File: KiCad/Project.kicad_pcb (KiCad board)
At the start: 2 copper layers, 74.9 x 99.1 mm, 74 parts, among them IC1 ATMEGA328-P, IC2 ATTINY85-P, IC3 ATTINY85-P, M1 Motor, M2 Motor, P1 CONN_02X03, P2 CONN_01X02, P3 CONN_01X02, P4 CONN_01X02, P5 CONN_02X04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

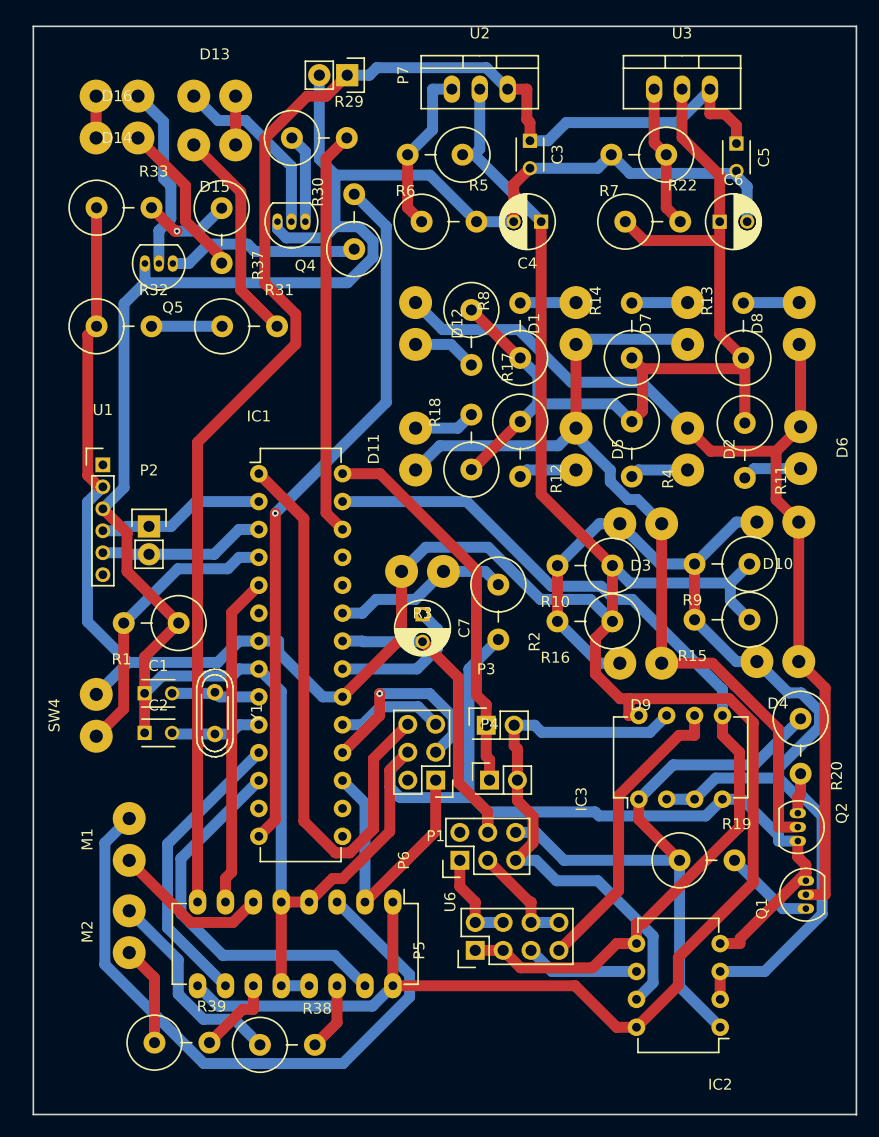
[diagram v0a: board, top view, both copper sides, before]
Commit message: Updated code for BT pairing and modified vias in PCB
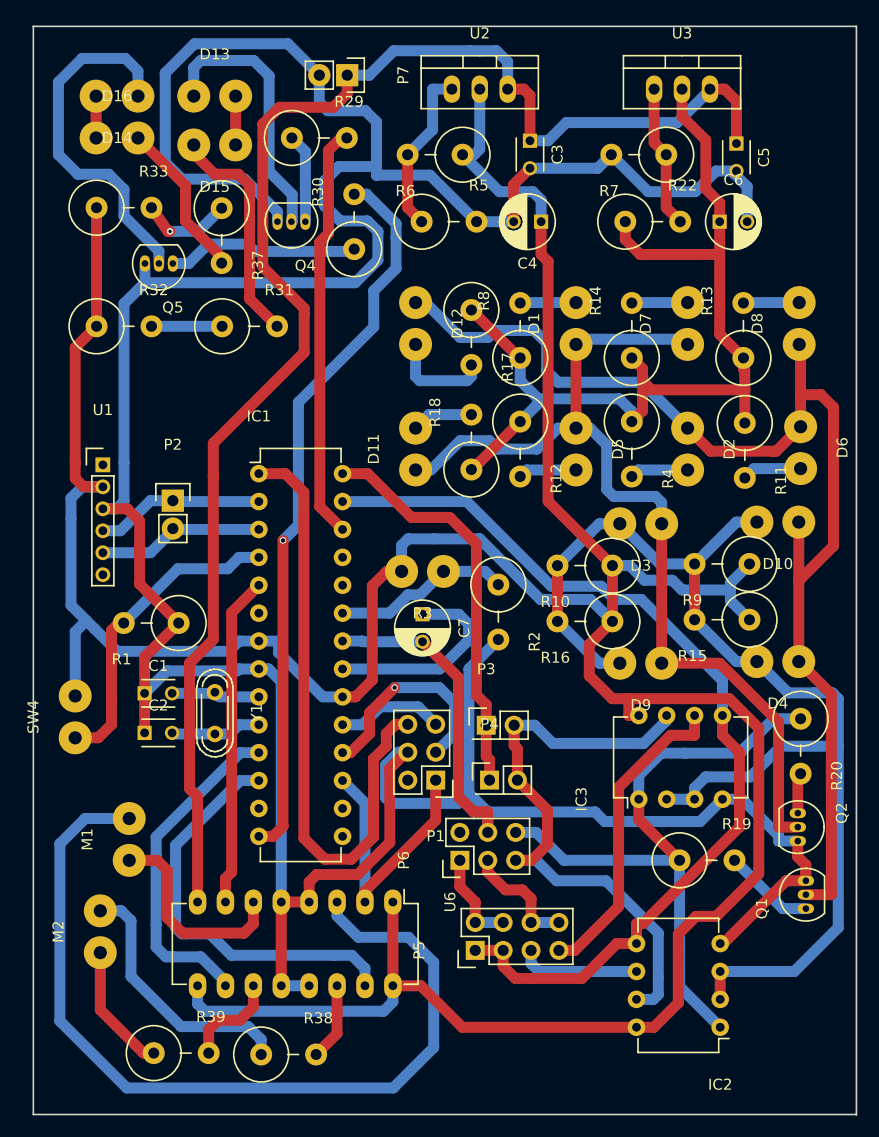
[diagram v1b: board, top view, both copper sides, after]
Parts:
- moved P2 3.19 mm to (64.8, 73.7)
- moved M2 2.63 mm to (58.2, 112.9)
- moved SW4 1.93 mm to (55.9, 93.3)
- moved R39 0.95 mm to (65.5, 124.0)
- moved R38 0.89 mm to (75.3, 124.1)
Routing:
- net GND: track 312.9 -> 358.8 mm
- net /Motor/Vroom: track 59.6 -> 81.1 mm
- net /IR/5V: track 288.0 -> 306.3 mm
- net Net-(D10-Pad1): track 93.1 -> 110.3 mm
- net Net-(D14-Pad1): track 16.9 -> 32.8 mm
- net /IR/Signal: track 102.0 -> 110.3 mm
- net Net-(D13-Pad1): track 16.6 -> 24.5 mm
- net /Motor/9V: track 131.7 -> 137.6 mm
- net Net-(C7-Pad1): track 13.1 -> 18.6 mm
- net /Motor/Styrning: track 18.8 -> 23.8 mm
- net Net-(IC2-Pad7): track 50.2 -> 55.0 mm
- net Net-(M1-Pad1): track 14.4 -> 19.0 mm
- net Net-(D1-Pad1): track 83.1 -> 87.3 mm
- net Net-(IC1-Pad1): track 52.6 -> 56.5 mm
- net /Motor/Left: track 26.8 -> 30.7 mm
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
